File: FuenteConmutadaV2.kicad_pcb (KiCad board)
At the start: 2 copper layers, 80 x 40 mm, 32 parts, among them J1 USB_C_Receptacle_USB2.0, J2 Conn_01x01_Pin, J3 Conn_01x01_Pin, J4 Conn_01x01_Pin

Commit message: Optimización
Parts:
- moved R4 11.6 mm to (164.0, 104.0), turned to 0 degrees
- moved CP10 2.03 mm to (149.6, 91.1), turned to -90 degrees
- moved R1 1.93 mm to (145.0, 89.2)
- moved L1 0.51 mm to (134.9, 89.4)
- moved MES1 0.25 mm to (125.3, 112.0)
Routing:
- net GND: track 10.7 -> 18.5 mm
- net Net-(Uw1-FB): track 28.5 -> 36.0 mm, vias 2 -> 1
- net Net-(Uw1-VDD): track 3.65 -> 7.48 mm
- net +5V: track 74.9 -> 76.7 mm
- net Net-(Uw1-EN): track 5.09 -> 3.58 mm
- net Net-(Uw1-BST): track 4.36 -> 4.93 mm

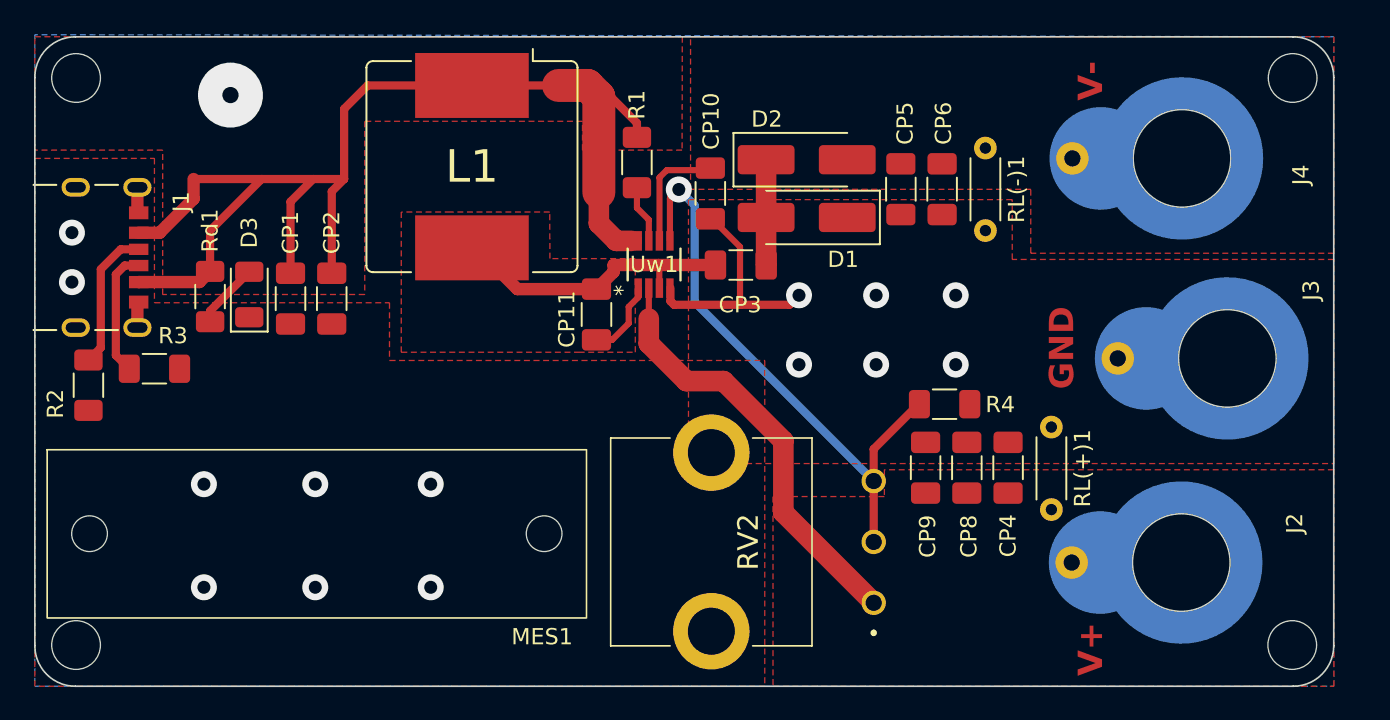
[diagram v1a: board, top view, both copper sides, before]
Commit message: Logos
Agregue logos en las capas de serigrafía
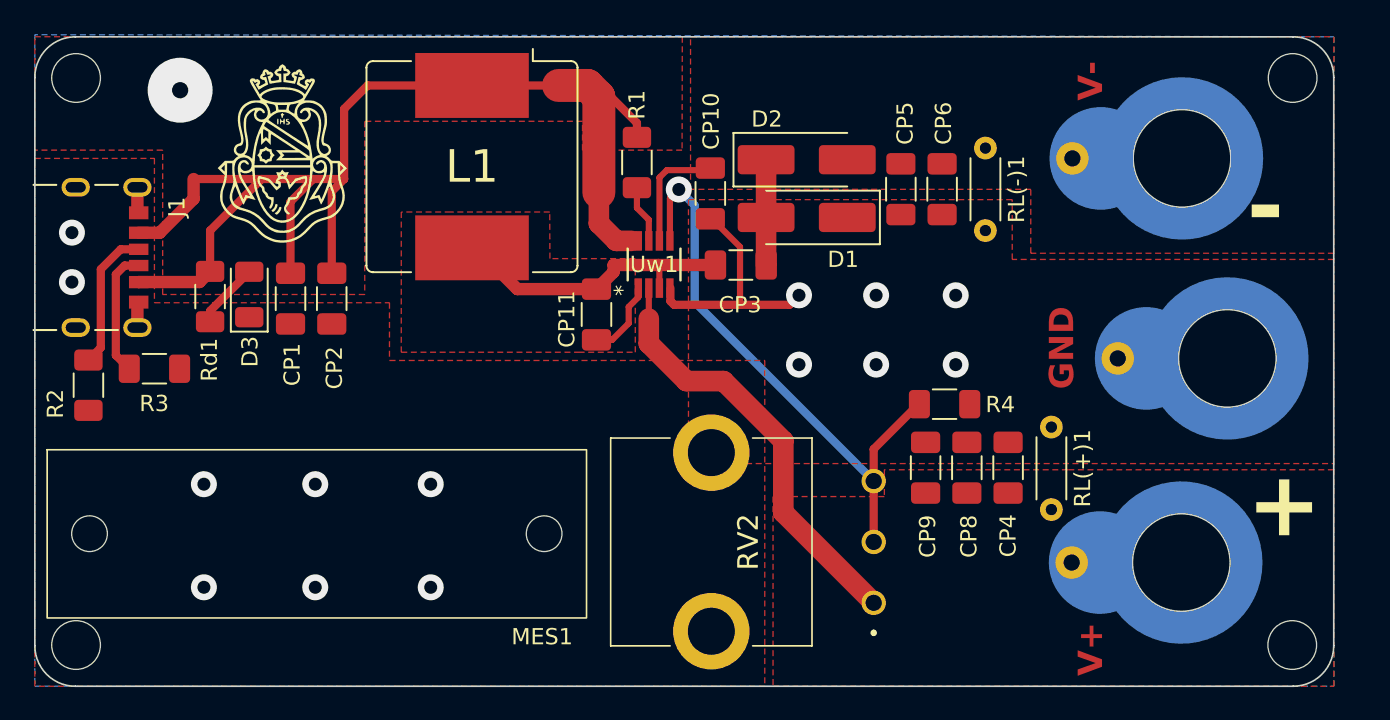
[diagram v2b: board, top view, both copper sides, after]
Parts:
- added G***: LOGO, Libreria_Propia:unc_logo_8x11mm, F.Cu at (123.2, 88.6)
- added TCdE FCEFYN: Logo, Taller:Logo, B.Cu at (133.6, 92.2)
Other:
- board text added: "+"
- board text added: "-"
